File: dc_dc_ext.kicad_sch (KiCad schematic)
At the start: 30 parts, among them U12 TPS56339DDC, U13 TPS56339DDC

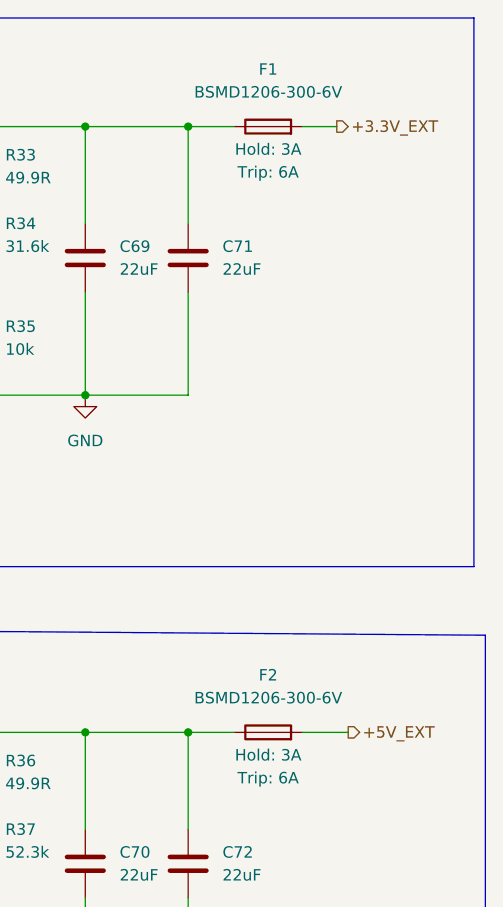
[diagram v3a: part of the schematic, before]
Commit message: fitted main schematics to A3, added few connectors and tuned power management section
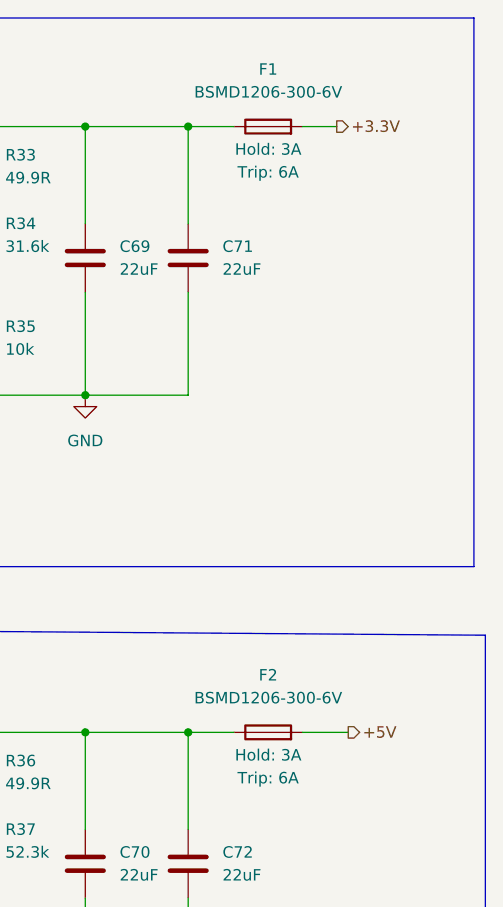
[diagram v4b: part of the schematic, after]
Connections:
- net +3.3V_EXT renamed +3.3V
- net +5V_EXT renamed +5V
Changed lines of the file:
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@@
     (effects (font (size 1.27 1.27)) (justify right))
   )
-  (hierarchical_label "+5V_EXT" (shape output) (at 214.63 105.41 0)
+  (hierarchical_label "+5V" (shape output) (at 214.63 105.41 0)
     (effects (font (size 1.27 1.27)) (justify left))
   )
-  (hierarchical_label "+3.3V_EXT" (shape output) (at 213.36 38.1 0)
+  (hierarchical_label "+3.3V" (shape output) (at 213.36 38.1 0)
     (effects (font (size 1.27 1.27)) (justify left))
   )

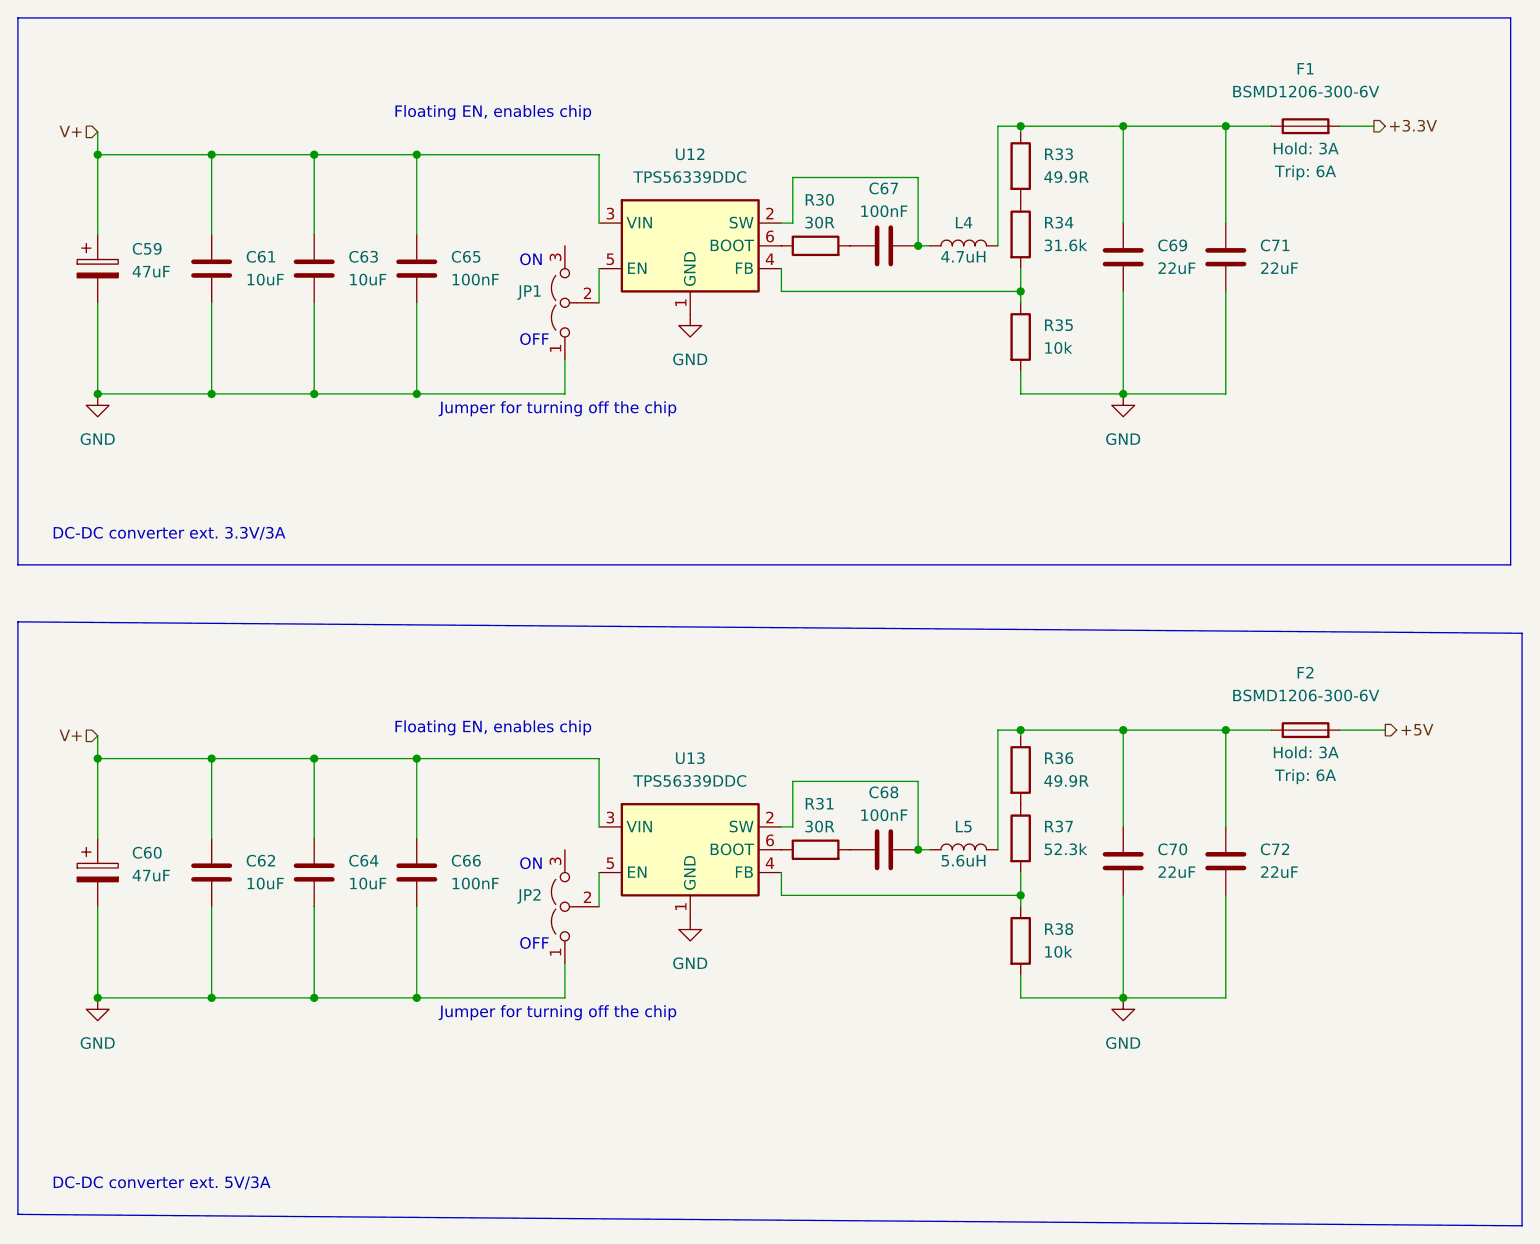
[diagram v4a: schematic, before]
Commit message: replaced main MCU, reannotated
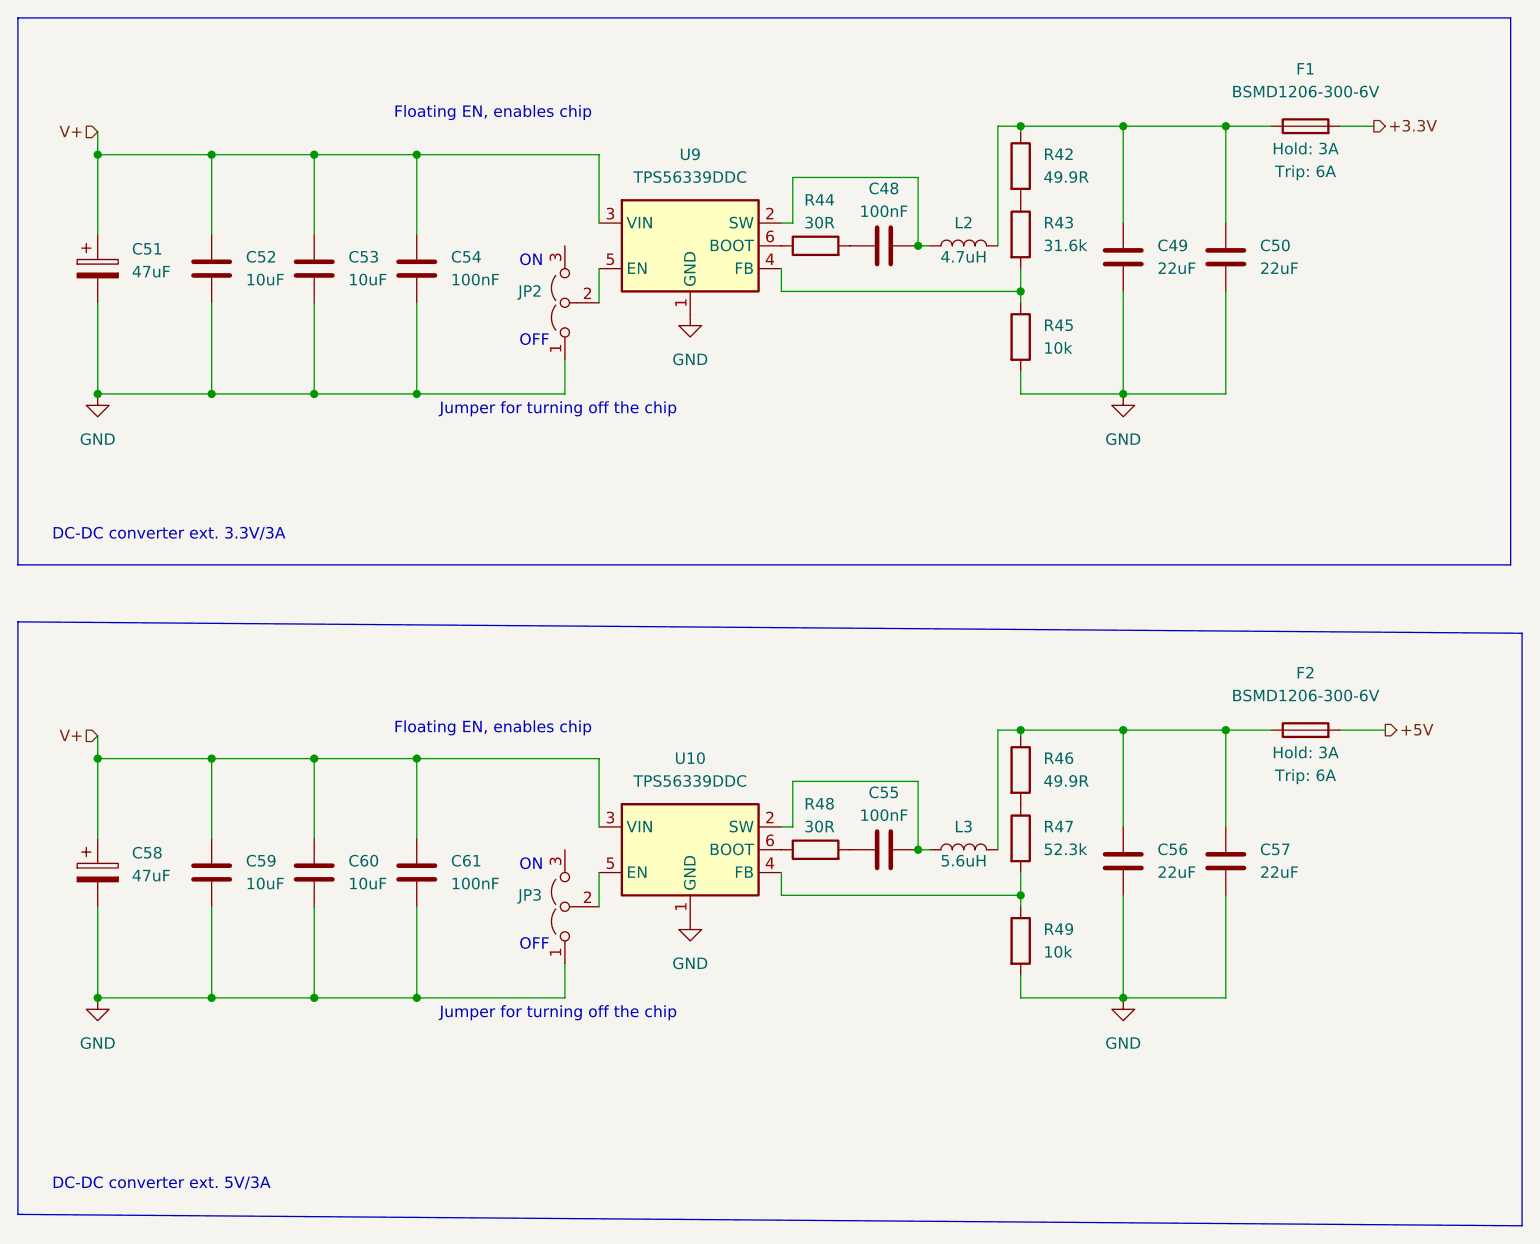
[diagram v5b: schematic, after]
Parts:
- renumbered C67 to C48, C69 to C49, C71 to C50, C59 to C51, C61 to C52, C63 to C53, C65 to C54, C68 to C55, C70 to C56, C72 to C57, C60 to C58, C62 to C59, C64 to C60, C66 to C61, JP1 to JP2, JP2 to JP3, L4 to L2, L5 to L3, R33 to R42, R34 to R43, R30 to R44, R35 to R45, R36 to R46, R37 to R47, R31 to R48, R38 to R49, U13 to U10, U12 to U9

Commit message: resolved all erc errors
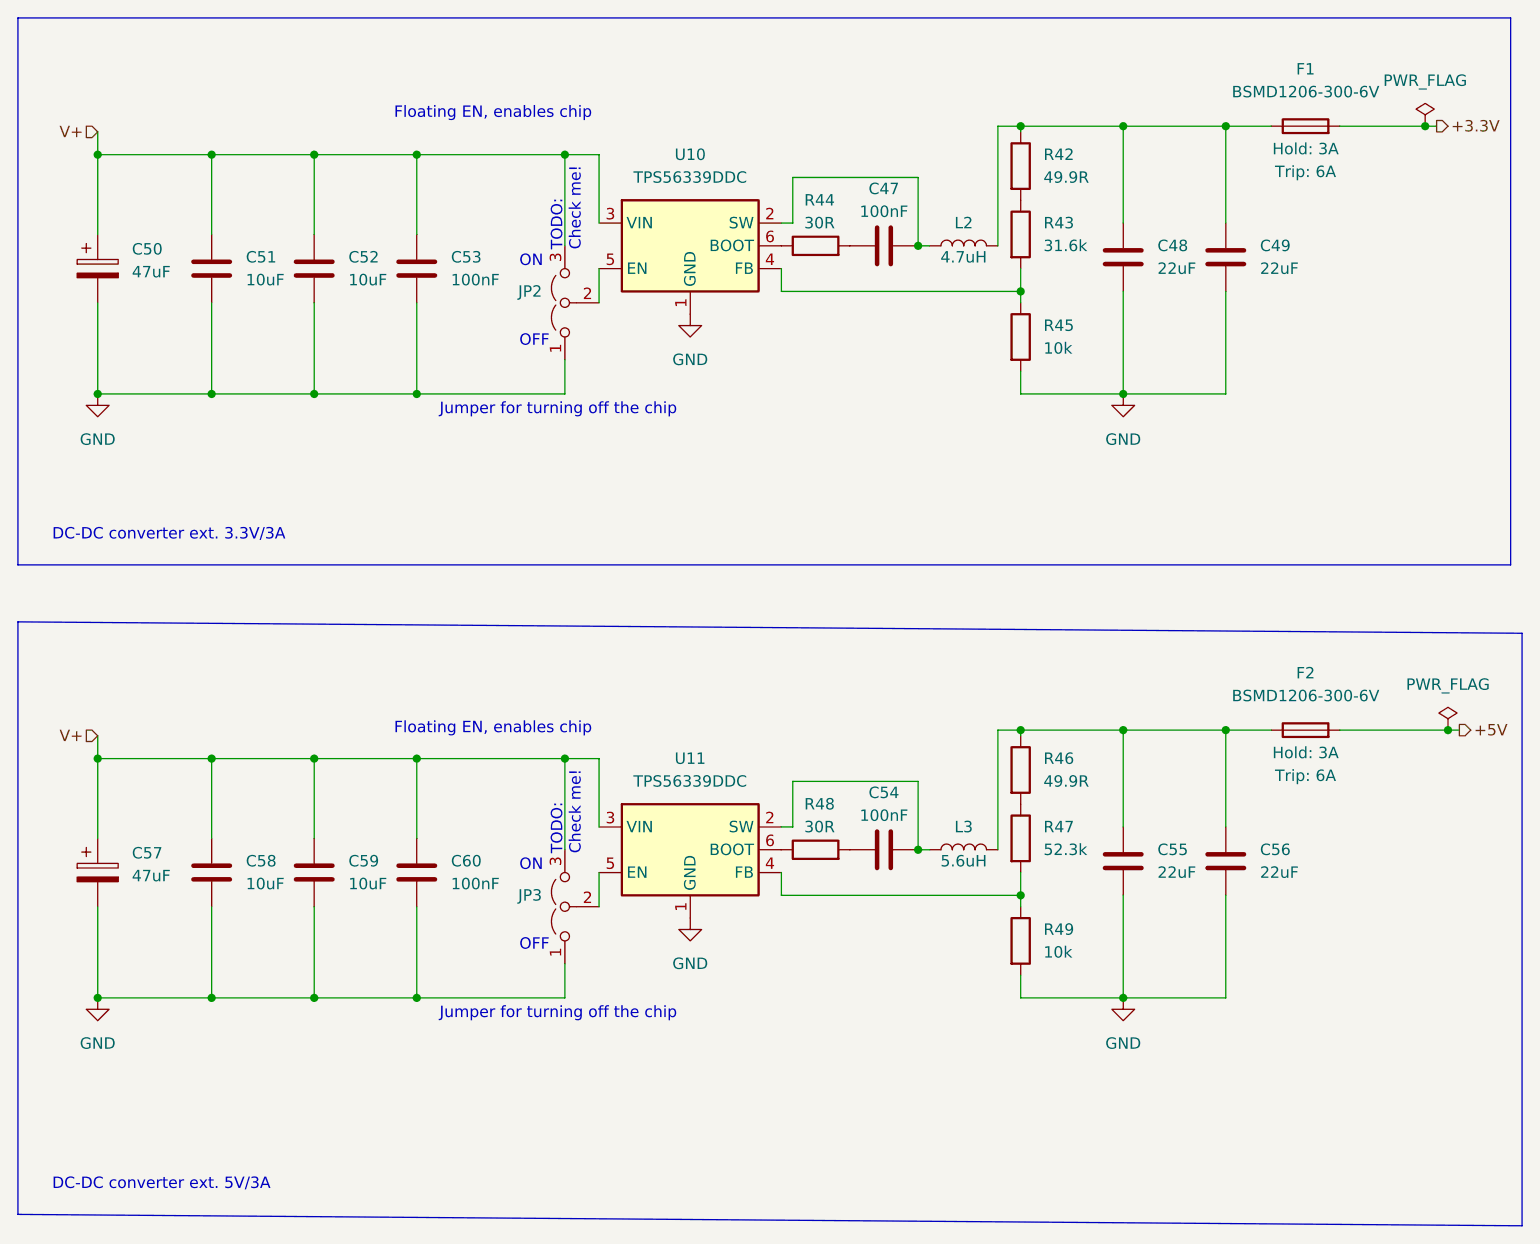
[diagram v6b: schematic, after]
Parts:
- renumbered C48 to C47, C49 to C48, C50 to C49, C51 to C50, C52 to C51, C53 to C52, C54 to C53, C55 to C54, C56 to C55, C57 to C56, C58 to C57, C59 to C58, C60 to C59, C61 to C60, U9 to U10, U10 to U11
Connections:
- net V+: now also JP2.3 (B), JP3.3 (B)
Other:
- note added: "TODO: Check me!"

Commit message: updated footprints from schematics
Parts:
- C47, C53, C54, C60: LCSC (none) -> C49678
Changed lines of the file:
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@@
       (effects (font (size 1.27 1.27)) hide)
     )
-    (property "Datasheet" "~" (id 3) (at 106.68 121.285 0)
+    (property "Datasheet" "https://datasheet.lcsc.com/lcsc/1810101813_YAGEO-CC0805KRX7R9BB104_C49678.pdf" (id 3) (at 106.68 121.285 0)
+      (effects (font (size 1.27 1.27)) hide)
+    )
+    (property "LCSC" "C49678" (id 4) (at 106.68 121.285 0)
       (effects (font (size 1.27 1.27)) hide)
     )
@@
       (effects (font (size 1.27 1.27)) hide)
     )
-    (property "Datasheet" "~" (id 3) (at 158.75 51.435 0)
+    (property "Datasheet" "https://datasheet.lcsc.com/lcsc/1810101813_YAGEO-CC0805KRX7R9BB104_C49678.pdf" (id 3) (at 158.75 51.435 0)
+      (effects (font (size 1.27 1.27)) hide)
+    )
+    (property "LCSC" "C49678" (id 4) (at 158.75 51.435 0)
       (effects (font (size 1.27 1.27)) hide)
     )
@@
       (effects (font (size 1.27 1.27)) hide)
     )
-    (property "Datasheet" "~" (id 3) (at 158.75 118.745 0)
+    (property "Datasheet" "https://datasheet.lcsc.com/lcsc/1810101813_YAGEO-CC0805KRX7R9BB104_C49678.pdf" (id 3) (at 158.75 118.745 0)
+      (effects (font (size 1.27 1.27)) hide)
+    )
+    (property "LCSC" "C49678" (id 4) (at 158.75 118.745 0)
       (effects (font (size 1.27 1.27)) hide)
     )
@@
       (effects (font (size 1.27 1.27)) hide)
     )
-    (property "Datasheet" "~" (id 3) (at 106.68 53.975 0)
-      (effects (font (size 1.27 1.27)) hide)
-    )
+    (property "Datasheet" "https://datasheet.lcsc.com/lcsc/1810101813_YAGEO-CC0805KRX7R9BB104_C49678.pdf" (id 3) (at 106.68 53.975 0)
+      (effects (font (size 1.27 1.27)) hide)
+    )
+    (property "LCSC" "C49678" (id 4) (at 106.68 53.975 0)
+      (effects (font (size 1.27 1.27)) hide)
+    )
